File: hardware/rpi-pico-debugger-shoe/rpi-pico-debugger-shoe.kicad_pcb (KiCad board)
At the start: 2 copper layers, 25.4 x 54.5 mm, 49 parts, among them J1 10118193-0001LF, J2 Conn_01x02, J3 Conn_01x03, J4 Conn_01x18, J5 Conn_01x20, J6 Conn_01x03, J7 Conn_01x03, J8 Conn_01x02, SW1 PTS810_SJK_250_SMTR_LFS, U1 RP2040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

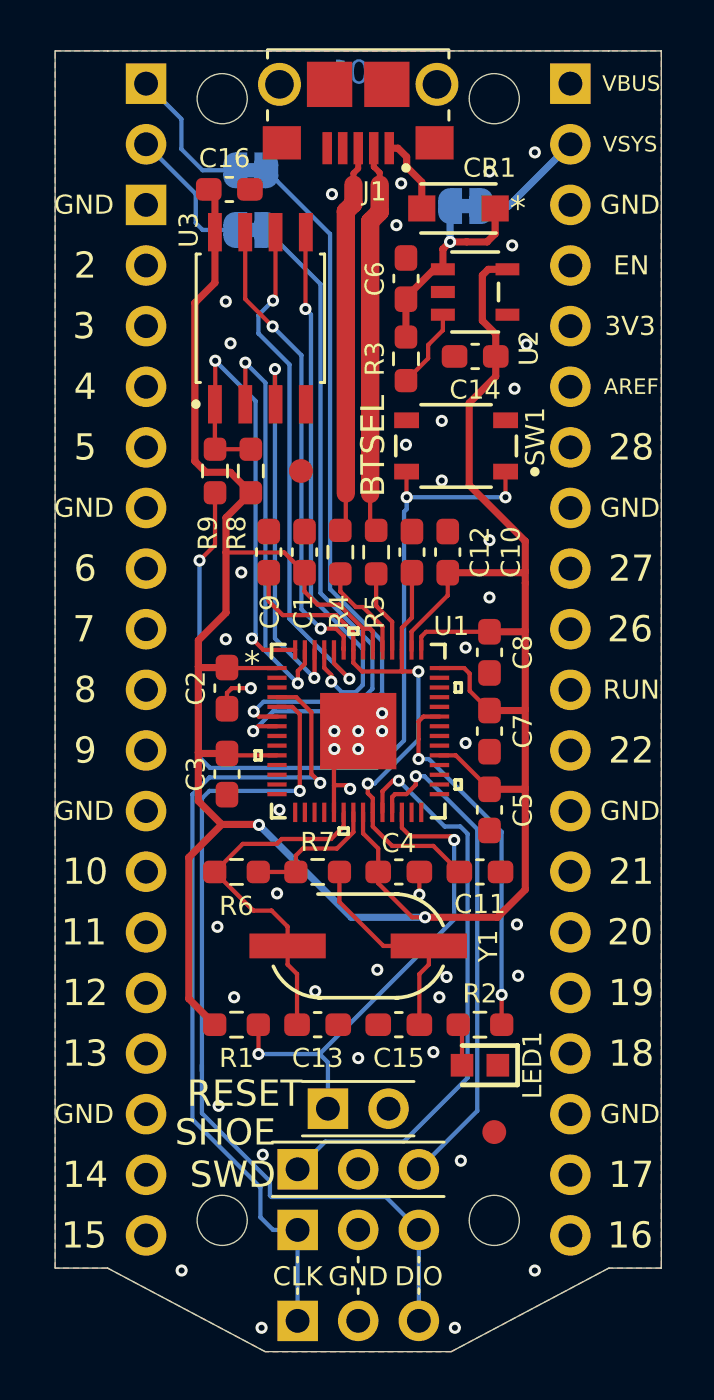
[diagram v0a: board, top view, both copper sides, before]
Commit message: Swapped R8 and R9 silk because I messed that up in v01.
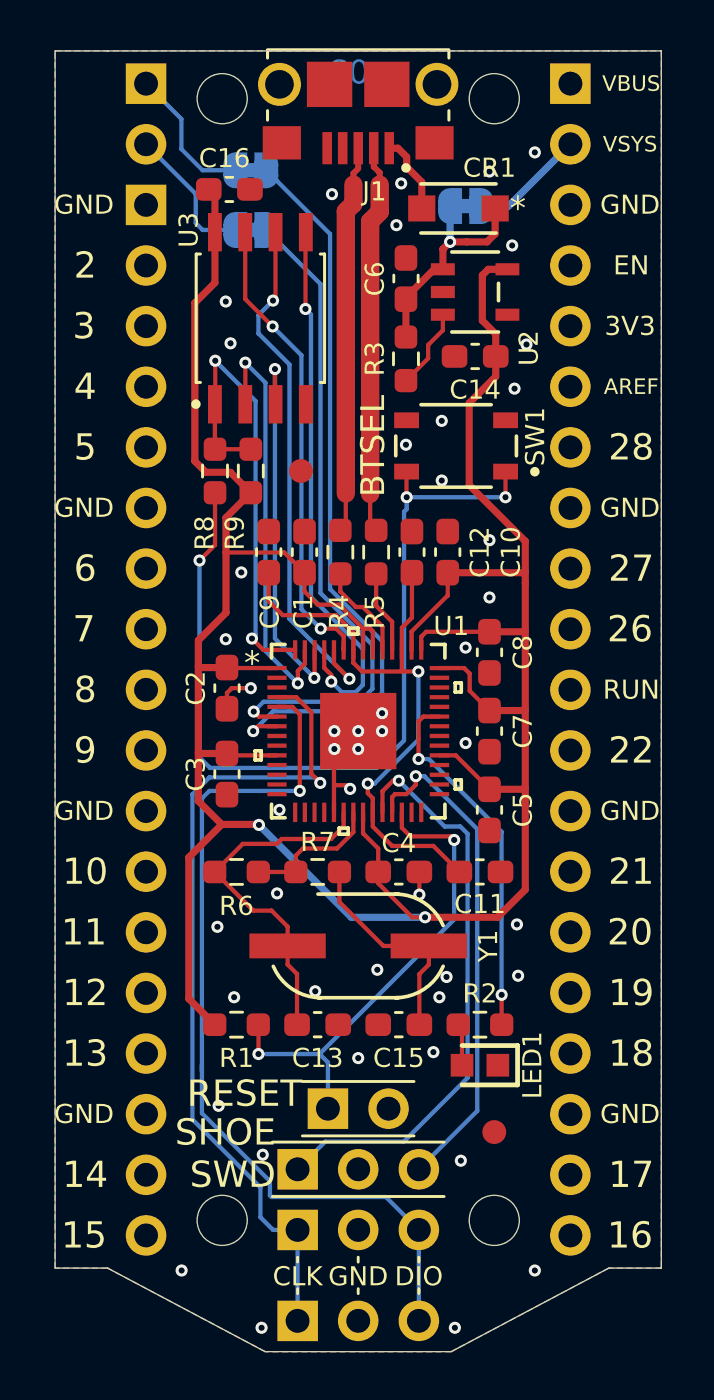
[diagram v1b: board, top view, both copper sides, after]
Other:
- board text added: "v02"
- board text removed: "v01"
